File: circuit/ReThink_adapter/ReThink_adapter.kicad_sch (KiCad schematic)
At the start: 78 parts, among them J1 FH34SRJ-34S-0.5SH(50), J10 OUT2, J11 OUT3, J2 FH34SRJ-6S-0.5SH(50), J3 Mezzanine, J4 XF3M(1)-3015-1B, J5 XF3M(1)-0815-1B, J6 FH34SRJ-40S-0.5SH(50), J7 FH52-40S-0.5SH, J8 XF3M(1)-1415-1B, J9 OUT1, U1 PCAL6416AHF, U2 LM2775DSG, U3 PCA9306, U4 TPS610333DRLR

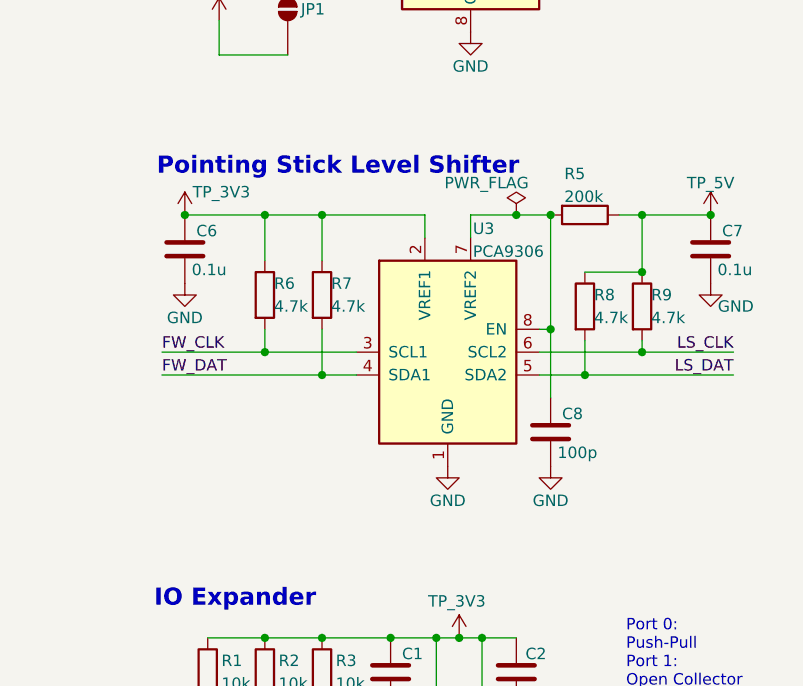
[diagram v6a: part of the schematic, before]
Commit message: added BOM
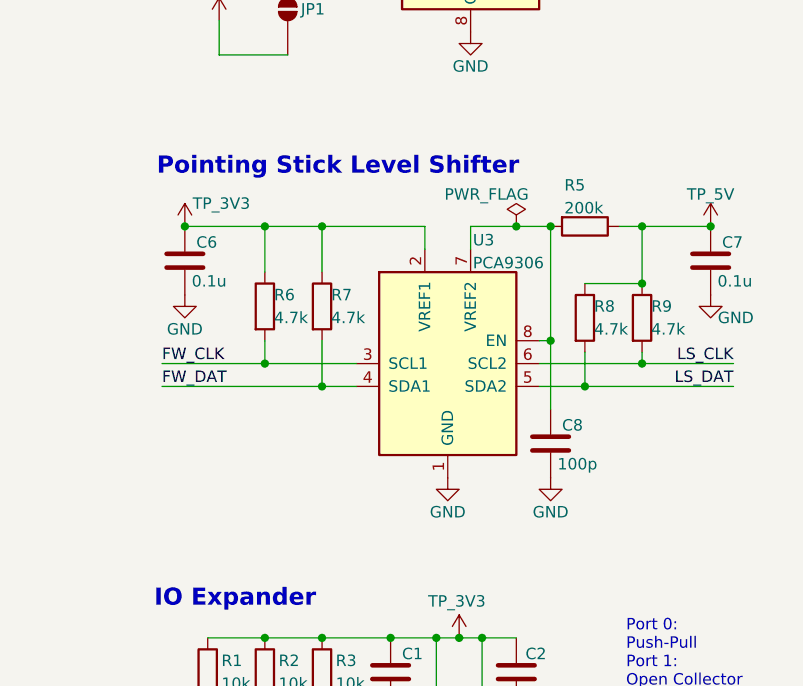
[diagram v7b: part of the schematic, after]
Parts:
- C1, C15, C17, C18, C2, C23, C6, C7: Distributor link (none) -> https://www.mouser.pl/en/ProductDetail/Murata-Electronics/G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; MPN (none) -> GRM155R71H104KE14D; RoHS (none) -> Compliant
- C10, C11, C3, C4, C9: Dielectric X7R -> X5R; Distributor link (none) -> https://www.mouser.pl/en/ProductDetail/Murata-Electronics/G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; MPN (none) -> GRM188R61E106MA73J; RoHS (none) -> Compliant
- C12, C13, C19, C20: Dielectric X7R -> X5R; Distributor link (none) -> https://www.mouser.pl/en/ProductDetail/Murata-Electronics/G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; MPN (none) -> GRM219R61C226ME15K; RoHS (none) -> Compliant; Voltage (none) -> 16; now in the parts list
- C14: Distributor link (none) -> https://www.mouser.pl/en/ProductDetail/Samsung-Electro-Mech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; MPN (none) -> CL05B103KB5NNNC; RoHS (none) -> Compliant
- C16, C21, C22: Distributor link (none) -> https://www.mouser.pl/en/ProductDetail/KEMET/C0402C221J2GAC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; MPN (none) -> C0402C221J2GACTU; RoHS (none) -> Compliant
- C5: Distributor link (none) -> https://www.mouser.pl/en/ProductDetail/TAIYO-YUDEN/MLAST168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; MPN (none) -> MLAST168SB7105KTNA01; RoHS (none) -> Compliant
- C8: Distributor link (none) -> https://www.mouser.pl/en/ProductDetail/Murata-Electronics/G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; MPN (none) -> GRM1555C2A101GA01D; RoHS (none) -> Compliant
- J1: Distributor link (none) -> https://www.mouser.pl/en/ProductDetail/Hirose-Connector/FH3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; MPN (none) -> FH34SRJ-34S-0.5SH(50); RoHS (none) -> Compliant
- J2: Distributor link (none) -> https://www.mouser.pl/en/ProductDetail/Hirose-Connector/FH3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; MPN (none) -> FH34SRJ-6S-0.5SH(50); RoHS (none) -> Compliant
- J3: Alt_MPN (none) -> 0543630489; Alt_link (none) -> https://www.digikey.pl/en/products/detail/molex/0543630489/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; Distributor link (none) -> https://www.questcomp.com/part/4/aa01b-s040va1-r3000/434153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; MPN (none) -> AA01B-S040VA1; RoHS (none) -> UNKNOWN
- J4: Distributor link (none) -> https://www.mouser.pl/en/ProductDetail/Omron-Electronics/XF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; MPN (none) -> XF3M(1)-3015-1B; RoHS (none) -> Compliant
- J5: Distributor link (none) -> https://www.mouser.pl/en/ProductDetail/Omron-Electronics/XF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; MPN (none) -> XF3M(1)-0815-1B; RoHS (none) -> Compliant
- J6: Distributor link (none) -> https://www.mouser.pl/en/ProductDetail/Hirose-Connector/FH3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; MPN (none) -> FH34SRJ-40S-0.5SH(50); RoHS (none) -> Compliant
- J7: Distributor link (none) -> https://www.mouser.pl/en/ProductDetail/Hirose-Connector/FH5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; MPN (none) -> FH52-40S-0.5SH; RoHS (none) -> Compliant
- J8: Distributor link (none) -> https://www.mouser.pl/en/ProductDetail/Omron-Electronics/XF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; MPN (none) -> XF3M(1)-1415-1B; RoHS (none) -> Compliant
- L1: Distributor link (none) -> https://www.mouser.pl/en/ProductDetail/Vishay-Dale/IHHP0806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; RoHS (none) -> Compliant; now in the parts list
- R1, R14, R2, R22, R23, R3, R4: Distributor link (none) -> https://www.mouser.pl/en/ProductDetail/YAGEO/RC0402FR-0710K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; MPN (none) -> RC0402FR-0710KP; RoHS (none) -> Compliant
- R10: Distributor link (none) -> https://www.mouser.pl/en/ProductDetail/YAGEO/RC0402FR-072K2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; MPN (none) -> RC0402FR-072K2P; RoHS (none) -> Compliant
- R11: Distributor link (none) -> https://www.mouser.pl/en/ProductDetail/YAGEO/RC0402FR-07560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; MPN (none) -> RC0402FR-07560RL; RoHS (none) -> Exemption
- R12: Distributor link (none) -> https://www.mouser.pl/en/ProductDetail/YAGEO/RC0402FR-07220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; MPN (none) -> RC0402FR-07220RP; RoHS (none) -> Compliant
- R13: Distributor link (none) -> https://www.mouser.pl/en/ProductDetail/YAGEO/RC0402FR-07330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; MPN (none) -> RC0402FR-07330RL; RoHS (none) -> Exemption
- R15, R16: Distributor link (none) -> https://www.mouser.pl/en/ProductDetail/YAGEO/RC0402FR-073K9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; MPN (none) -> RC0402FR-073K9L; RoHS (none) -> Exemption
- R17, R18, R19, R20, R21: Distributor link (none) -> https://www.mouser.pl/en/ProductDetail/YAGEO/RC0402FR-07100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; MPN (none) -> RC0402FR-07100RP; RoHS (none) -> Compliant
- R24: Distributor link (none) -> https://www.mouser.pl/en/ProductDetail/YAGEO/RC0402FR-07100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; MPN (none) -> RC0402FR-07100KP; RoHS (none) -> Compliant
- R5: Distributor link (none) -> https://www.mouser.pl/en/ProductDetail/YAGEO/RC0402FR-07200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; MPN (none) -> RC0402FR-07200KP; RoHS (none) -> Compliant
- R6, R7, R8, R9: Distributor link (none) -> https://www.mouser.pl/en/ProductDetail/YAGEO/RC0402FR-074K7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; MPN (none) -> RC0402FR-074K7P; RoHS (none) -> Compliant
- U1: Distributor link (none) -> https://www.mouser.pl/en/ProductDetail/NXP-Semiconductors/P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; MPN (none) -> PCAL6416AHF,128; RoHS (none) -> Compliant
- U2: Distributor link (none) -> https://www.mouser.pl/en/ProductDetail/Texas-Instruments/LM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; MPN (none) -> LM2775DSGT; RoHS (none) -> Compliant
- U3: Distributor link (none) -> https://www.mouser.pl/en/ProductDetail/Texas-Instruments/PC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; MPN (none) -> PCA9306DCUR; RoHS (none) -> Compliant
- U4: Distributor link (none) -> https://www.mouser.pl/en/ProductDetail/Texas-Instruments/TP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; MPN (none) -> TPS610333DRLR; RoHS (none) -> Compliant
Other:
- moved on the sheet: C6, C7, C8, R5, R6, R7, R8, R9, U3

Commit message: add step 3d model, update BOM
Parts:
- C1, C15, C17, C18, C2, C23, C6, C7: Alt_link (none) -> https://www.digikey.pl/en/products/detail/murata-electronic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; DigiKey_PN (none) -> 490-10700-1-ND; Mouser_PN (none) -> 81-GRM155R71H104KE4D
- C10, C11, C3, C4, C9: Alt_link (none) -> https://www.digikey.pl/en/products/detail/samsung-electro-m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; DigiKey_PN (none) -> 1276-1869-1-ND; Mouser_PN (none) -> 81-GRM188R61E106MA3J
- C12, C13, C19, C20: Alt_link (none) -> https://www.digikey.pl/en/products/detail/murata-electronic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; DigiKey_PN (none) -> 490-GRM219R61C226ME15KCT-ND; Mouser_PN (none) -> 81-GRM219R61C226ME1K
- C14: Alt_link (none) -> https://www.digikey.pl/en/products/detail/samsung-electro-m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; DigiKey_PN (none) -> 1276-1028-1-ND; Mouser_PN (none) -> 187-CL05B103KB5NNNC
- C16, C21, C22: Alt_link (none) -> https://www.digikey.pl/en/products/detail/kemet/C0402C221J2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; DigiKey_PN (none) -> 399-C0402C221J2GACTUCT-ND; Mouser_PN (none) -> 80-C0402C221J2GACTU
- C5: Alt_link (none) -> https://www.digikey.pl/en/products/detail/taiyo-yuden/MLAST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; DigiKey_PN (none) -> 587-MLAST168SB7105KTNA01CT-ND; Mouser_PN (none) -> 963-MLAST168SB7105KT
- C8: Alt_link (none) -> https://www.digikey.pl/en/products/detail/murata-electronic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; DigiKey_PN (none) -> 490-GRM1555C2A101GA01DCT-ND; Mouser_PN (none) -> 81-GRM1555C2A101GA1D
- J1: Alt_link (none) -> https://www.digikey.pl/en/products/detail/hirose-electric-c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; DigiKey_PN (none) -> 26-FH34SRJ-34S-0.5SH(50)CT-ND; Mouser_PN (none) -> 798-FH34SRJ34S05SH50
- J10, J11, J9: now not fitted
- J2: Alt_link (none) -> https://www.digikey.pl/en/products/detail/hirose-electric-c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; DigiKey_PN (none) -> H125773CT-ND; Mouser_PN (none) -> 798-FH34SRJ6S05SH50
- J3: DigiKey_PN (none) -> WM6787CT-ND
- J4: Alt_link (none) -> https://www.digikey.pl/en/products/detail/aratas-formerly-o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; DigiKey_PN (none) -> OR1179CT-ND; Mouser_PN (none) -> 653-XF3M1-3015-1B
- J5: Alt_link (none) -> https://www.digikey.pl/en/products/detail/aratas-formerly-o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; DigiKey_PN (none) -> OR1222CT-ND; Mouser_PN (none) -> 653-XF3M108151B
- J6: Alt_link (none) -> https://www.digikey.pl/en/products/detail/hirose-electric-c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; DigiKey_PN (none) -> H125755CT-ND; Mouser_PN (none) -> 798-FH34SRJ40S05SH50
- J7: Alt_link (none) -> https://www.digikey.pl/en/products/detail/hirose-electric-c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; DigiKey_PN (none) -> HFZ040CT-ND; Mouser_PN (none) -> 798-FH5240S0.5SH
- J8: Alt_link (none) -> https://www.digikey.pl/en/products/detail/aratas-formerly-o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; DigiKey_PN (none) -> Z5875CT-ND; Mouser_PN (none) -> 653-XF3M114151B
- L1: Alt_link (none) -> https://www.digikey.pl/en/products/detail/vishay-dale/IHHP0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; DigiKey_PN (none) -> 541-IHHP0806ZHER1R0M01CT-ND; Mouser_PN (none) -> 70-IHHP0806ZHR1R0M01
- R1, R14, R2, R22, R23, R3, R4: Alt_link (none) -> https://www.digikey.pl/en/products/detail/yageo/RC0402FR-07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; DigiKey_PN (none) -> YAG1249CT-ND; Mouser_PN (none) -> 603-RC0402FR-0710KP
- R10: Alt_link (none) -> https://www.digikey.pl/en/products/detail/yageo/RC0402FR-07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; DigiKey_PN (none) -> YAG1260CT-ND; Mouser_PN (none) -> 603-RC0402FR-072K2P
- R11: Alt_link (none) -> https://www.digikey.pl/en/products/detail/yageo/RC0402FR-07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; DigiKey_PN (none) -> 311-560LRCT-ND; Mouser_PN (none) -> 603-RC0402FR-07560RL
- R12: Alt_link (none) -> https://www.digikey.pl/en/products/detail/yageo/RC0402FR-07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; DigiKey_PN (none) -> 13-RC0402FR-07220RPCT-ND; Mouser_PN (none) -> 603-RC0402FR-07220RP
- R13: Alt_link (none) -> https://www.digikey.pl/en/products/detail/yageo/RC0402FR-07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; DigiKey_PN (none) -> 311-330LRCT-ND; Mouser_PN (none) -> 603-RC0402FR-07330RL
- R15, R16: Alt_link (none) -> https://www.digikey.pl/en/products/detail/yageo/RC0402FR-07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; DigiKey_PN (none) -> 311-3.90KLRCT-ND; Mouser_PN (none) -> 603-RC0402FR-073K9L
- R17, R18, R19, R20, R21: Alt_link (none) -> https://www.digikey.pl/en/products/detail/yageo/RC0402FR-07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; DigiKey_PN (none) -> YAG1248CT-ND; Mouser_PN (none) -> 603-RC0402FR-07100RP
- R24: Alt_link (none) -> https://www.digikey.pl/en/products/detail/yageo/RC0402FR-07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; DigiKey_PN (none) -> 13-RC0402FR-07100KPCT-ND; Mouser_PN (none) -> 603-RC0402FR-07100KP
- R5: Alt_link (none) -> https://www.digikey.pl/en/products/detail/yageo/RC0402FR-07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; DigiKey_PN (none) -> 13-RC0402FR-07200KPCT-ND; Mouser_PN (none) -> 603-RC0402FR-07200KP
- R6, R7, R8, R9: Alt_link (none) -> https://www.digikey.pl/en/products/detail/yageo/RC0402FR-07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; DigiKey_PN (none) -> YAG1272CT-ND; Mouser_PN (none) -> 603-RC0402FR-074K7P
- U1: Alt_link (none) -> https://www.digikey.pl/en/products/detail/nxp-usa-inc/PCAL6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; DigiKey_PN (none) -> 568-9946-1-ND; Mouser_PN (none) -> 771-PCAL6416AHF,128
- U2: Alt_link (none) -> https://www.digikey.pl/en/products/detail/texas-instruments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; DigiKey_PN (none) -> 296-42149-1-ND; Mouser_PN (none) -> 595-LM2775DSGT
- U3: Alt_link (none) -> https://www.digikey.pl/en/products/detail/texas-instruments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; DigiKey_PN (none) -> 296-17988-1-ND; Mouser_PN (none) -> 595-PCA9306DCUR
- U4: Alt_link (none) -> https://www.digikey.pl/en/products/detail/texas-instruments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; DigiKey_PN (none) -> 296-TPS610333DRLRCT-ND; Mouser_PN (none) -> 595-TPS610333DRLR
